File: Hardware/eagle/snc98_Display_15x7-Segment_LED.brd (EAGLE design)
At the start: 154.9 x 33.5 mm, 68 parts, among them M10 IRLML6402, M11 IRLML6402, M4 IRLML6402, M5 IRLML6402, M6 IRLML6402, M7 IRLML6402, M8 IRLML6402, M9 IRLML6402, X1 MICROMATCH-12, X3 MICROMATCH-12

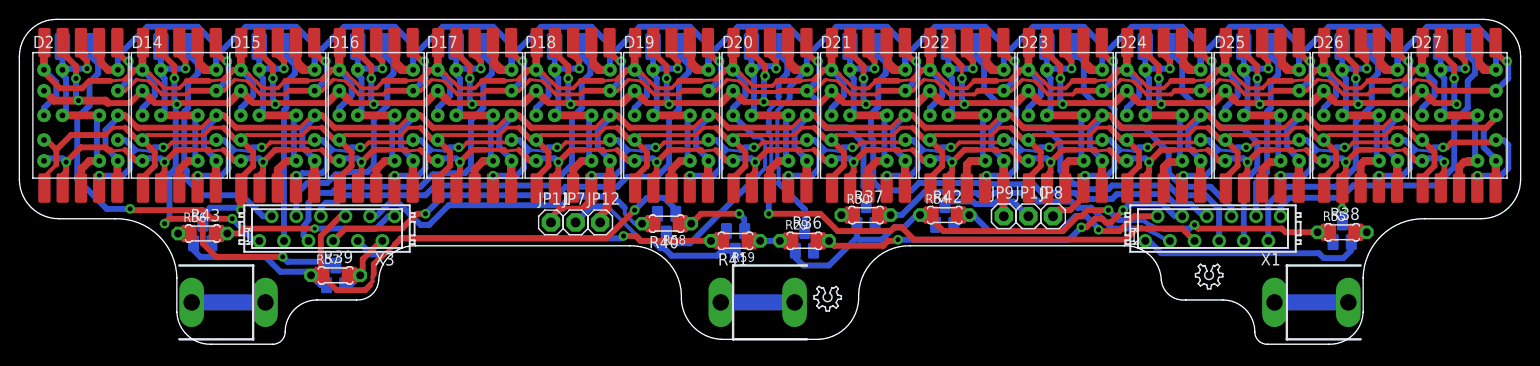
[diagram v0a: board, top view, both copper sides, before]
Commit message: PCB_Display_cleanup
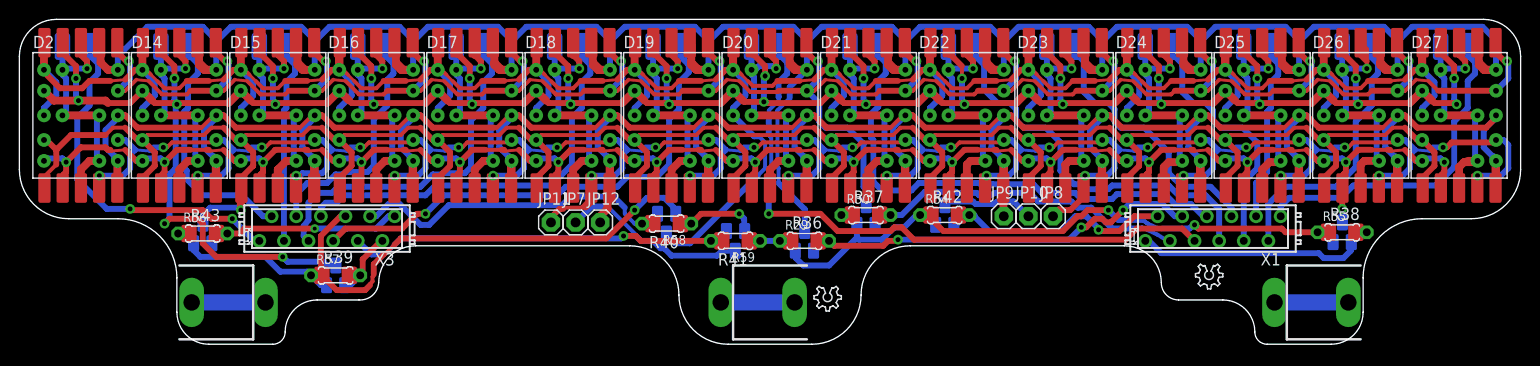
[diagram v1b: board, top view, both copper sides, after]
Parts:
- moved LOGO1 0.57 mm to (74.1, 6.91)
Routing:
- net SEG_A: track 335.7 -> 316.3 mm
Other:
- outline, holes or cut-outs redrawn
- board text added: "https:/ /oshpark.com"
- board text removed: "https://oshpark.com/"

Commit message: snc98_Display_15x7-Segment_LED_v2
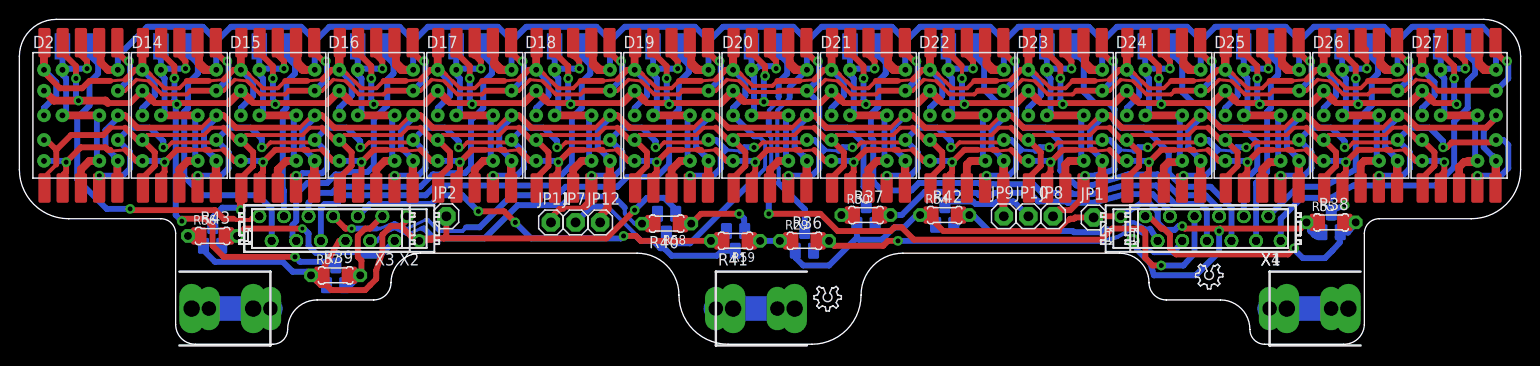
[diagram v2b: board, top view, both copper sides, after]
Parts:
- added JP1, JP2: (no value), adafruit:1X01
- added X2, X4: MICROMATCH-14, Con-amp-micromatch:MICROMATCH-14
- moved LOGO1 6.04 mm to (68.2, 8.43)
- moved M7 1.53 mm to (135.4, 12.6)
- moved R38 1.53 mm to (135.4, 12.6)
- moved R55 1.53 mm to (135.4, 12.6)
- moved M8 1.05 mm to (19.9, 11.2)
- moved R43 1.05 mm to (19.9, 11.2)
- moved R56 1.05 mm to (19.9, 11.2)
- moved BH4 0.63 mm to (133.3, 3.68)
- moved BH5 0.63 mm to (76.2, 3.68)
- moved BH6 0.63 mm to (21.6, 3.68)
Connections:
- net CA_LED: now also JP1.1, JP2.1, X2.13, X2.14, X2.8, X4.1, X4.2
- net D0_A: now also X2.1
- net D10_A: now also X4.10
- net D11_A: now also X4.11
- net D12_A: now also X4.12
- net D13_A: now also X4.13
- net D14_A: now also X4.14
- net D1_A: now also X2.2
- net D2_A: now also X2.3
- net D3_A: now also X2.4
- net D4_A: now also X2.5
- net D5_A: now also X2.6
- net D6_A: now also X2.7
- net D7_A: now also X4.7
- net D8_A: now also X4.8
- net D9_A: now also X4.9
- net IO-A: now also X4.6
- net IO-B: now also X4.5
- net IO-C: now also X4.4
- net IO-D: now also X4.3
- net IO-DP: now also X2.9
- net IO-E: now also X2.12
- net IO-F: now also X2.11
- net IO-G: now also X2.10
- net NC1: now also BH4.P3, BH4.P4
- net NC2: now also BH5.P3, BH5.P4
- net NC3: now also BH6.M3, BH6.M4
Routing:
- net CA_LED: track 164.2 -> 186.9 mm
- net SEG_C: track 271.7 -> 294.2 mm
- net D7_A: track 65.3 -> 72.2 mm, vias 1 -> 2
- net SEG_D: track 210.1 -> 206.6 mm
- net D13_A: track 28.2 -> 24.7 mm
- net D1_A: track 25.2 -> 28.1 mm
- net D8_A: track 52.1 -> 55.1 mm
- net IO-F: track 7.87 -> 10.8 mm
- net D4_A: track 36.3 -> 33.4 mm
- net D3_A: track 25.0 -> 27.9 mm
- net D5_A: track 42.0 -> 44.7 mm
- net IO-D: track 26.6 -> 29.3 mm, vias 0 -> 1
- net D12_A: track 18.8 -> 21.3 mm
- net D11_A: track 26.4 -> 23.8 mm
- net D10_A: track 28.3 -> 30.8 mm
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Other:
- outline, holes or cut-outs redrawn

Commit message: MR(); MS(); M+=(); Display Status
Display whe to or more switch pressed.
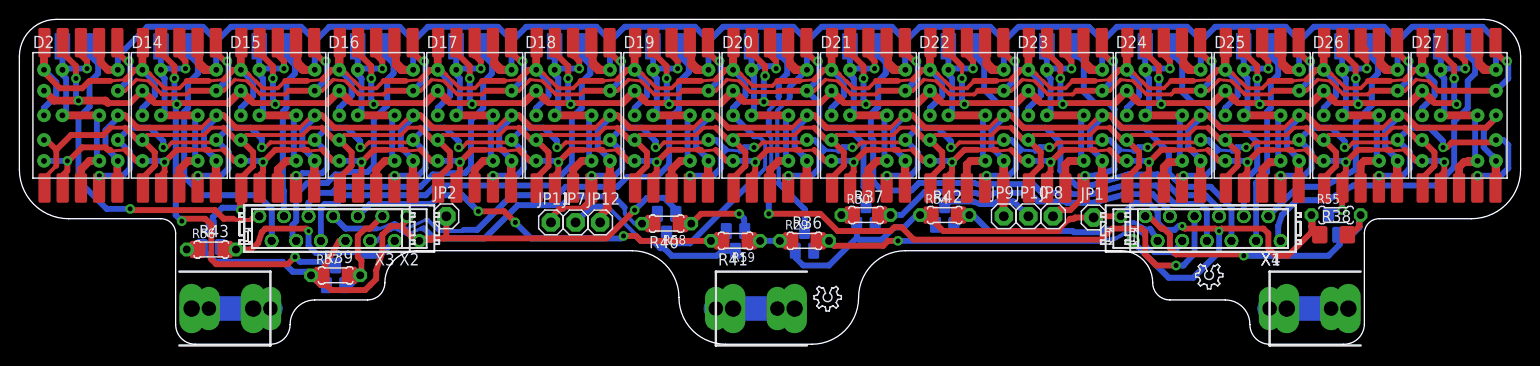
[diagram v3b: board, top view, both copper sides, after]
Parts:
- moved R43 1.40 mm to (19.8, 9.78)
- moved R56 1.40 mm to (19.8, 9.78)
- moved R38 1.30 mm to (135.6, 11.3)
- moved R55 0.92 mm to (135.9, 13.3)
- moved M7 0.36 mm to (135.1, 12.3)
- moved M8 0.18 mm to (19.8, 11.0)
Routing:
- net CA_LED: track 186.9 -> 192.9 mm
- net IO-D: track 29.3 -> 30.9 mm
- net SEG_F: track 305.1 -> 306.6 mm
- net IO-E: track 22.6 -> 23.3 mm
- net SEG_D: track 206.6 -> 207.2 mm
- net D6_A: vias 1 -> 0
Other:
- outline, holes or cut-outs redrawn

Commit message: New Hardware Design V0.4
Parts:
- M10, M11, M4, M5, M6, M7, M8, M9: value IRLML6402 -> IRLML2244
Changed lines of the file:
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@@
 <setting verticaltext="up"/>
 </settings>
-<grid distance="5" unitdist="mil" unit="mil" style="lines" multiple="1" display="yes" altdistance="0.01" altunitdist="inch" altunit="mil"/>
+<grid distance="0.1" unitdist="inch" unit="inch" style="lines" multiple="1" display="yes" altdistance="0.01" altunitdist="inch" altunit="inch"/>
 <layers>
-<layer number="1" name="Top" color="4" fill="1" visible="no" active="yes"/>
+<layer number="1" name="Top" color="4" fill="1" visible="yes" active="yes"/>
 <layer number="2" name="Route2" color="1" fill="3" visible="no" active="no"/>
 <layer number="3" name="Route3" color="4" fill="3" visible="no" active="no"/>
@@
 <element name="R18" library="rcl" package="R1210" value="22" x="137.922" y="30.734" rot="MR180"/>
 <element name="R19" library="rcl" package="R1210" value="22" x="148.082" y="30.734" rot="MR180"/>
-<element name="M4" library="IRLML6402" package="SOT-23" value="IRLML6402" x="81.026" y="10.668" rot="MR180"/>
-<element name="M5" library="IRLML6402" package="SOT-23" value="IRLML6402" x="87.376" y="13.335" rot="MR180"/>
-<element name="M6" library="IRLML6402" package="SOT-23" value="IRLML6402" x="95.504" y="13.335" rot="MR180"/>
-<element name="M7" library="IRLML6402" package="SOT-23" value="IRLML6402" x="135.128" y="12.319" rot="MR180"/>
-<element name="M8" library="IRLML6402" package="SOT-23" value="IRLML6402" x="19.812" y="11.049" rot="MR180"/>
-<element name="M9" library="IRLML6402" package="SOT-23" value="IRLML6402" x="32.639" y="7.112" rot="MR180"/>
-<element name="M10" library="IRLML6402" package="SOT-23" value="IRLML6402" x="66.802" y="12.446" rot="MR0"/>
-<element name="M11" library="IRLML6402" package="SOT-23" value="IRLML6402" x="73.914" y="10.668" rot="MR0"/>
+<element name="M4" library="IRLML6402" package="SOT-23" value="IRLML2244" x="81.026" y="10.668" rot="MR180"/>
+<element name="M5" library="IRLML6402" package="SOT-23" value="IRLML2244" x="87.376" y="13.335" rot="MR180"/>
+<element name="M6" library="IRLML6402" package="SOT-23" value="IRLML2244" x="95.504" y="13.335" rot="MR180"/>
+<element name="M7" library="IRLML6402" package="SOT-23" value="IRLML2244" x="135.128" y="12.319" rot="MR180"/>
+<element name="M8" library="IRLML6402" package="SOT-23" value="IRLML2244" x="19.812" y="11.049" rot="MR180"/>
+<element name="M9" library="IRLML6402" package="SOT-23" value="IRLML2244" x="32.639" y="7.112" rot="MR180"/>
+<element name="M10" library="IRLML6402" package="SOT-23" value="IRLML2244" x="66.802" y="12.446" rot="MR0"/>
+<element name="M11" library="IRLML6402" package="SOT-23" value="IRLML2244" x="73.914" y="10.668" rot="MR0"/>
 <element name="R36" library="rcl" package="R1206" value="3k3" x="81.026" y="10.668"/>
 <element name="R37" library="rcl" package="R1206" value="3k3" x="87.376" y="13.335"/>
